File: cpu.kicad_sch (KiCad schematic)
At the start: 1 part, among them U1 Intel_8088

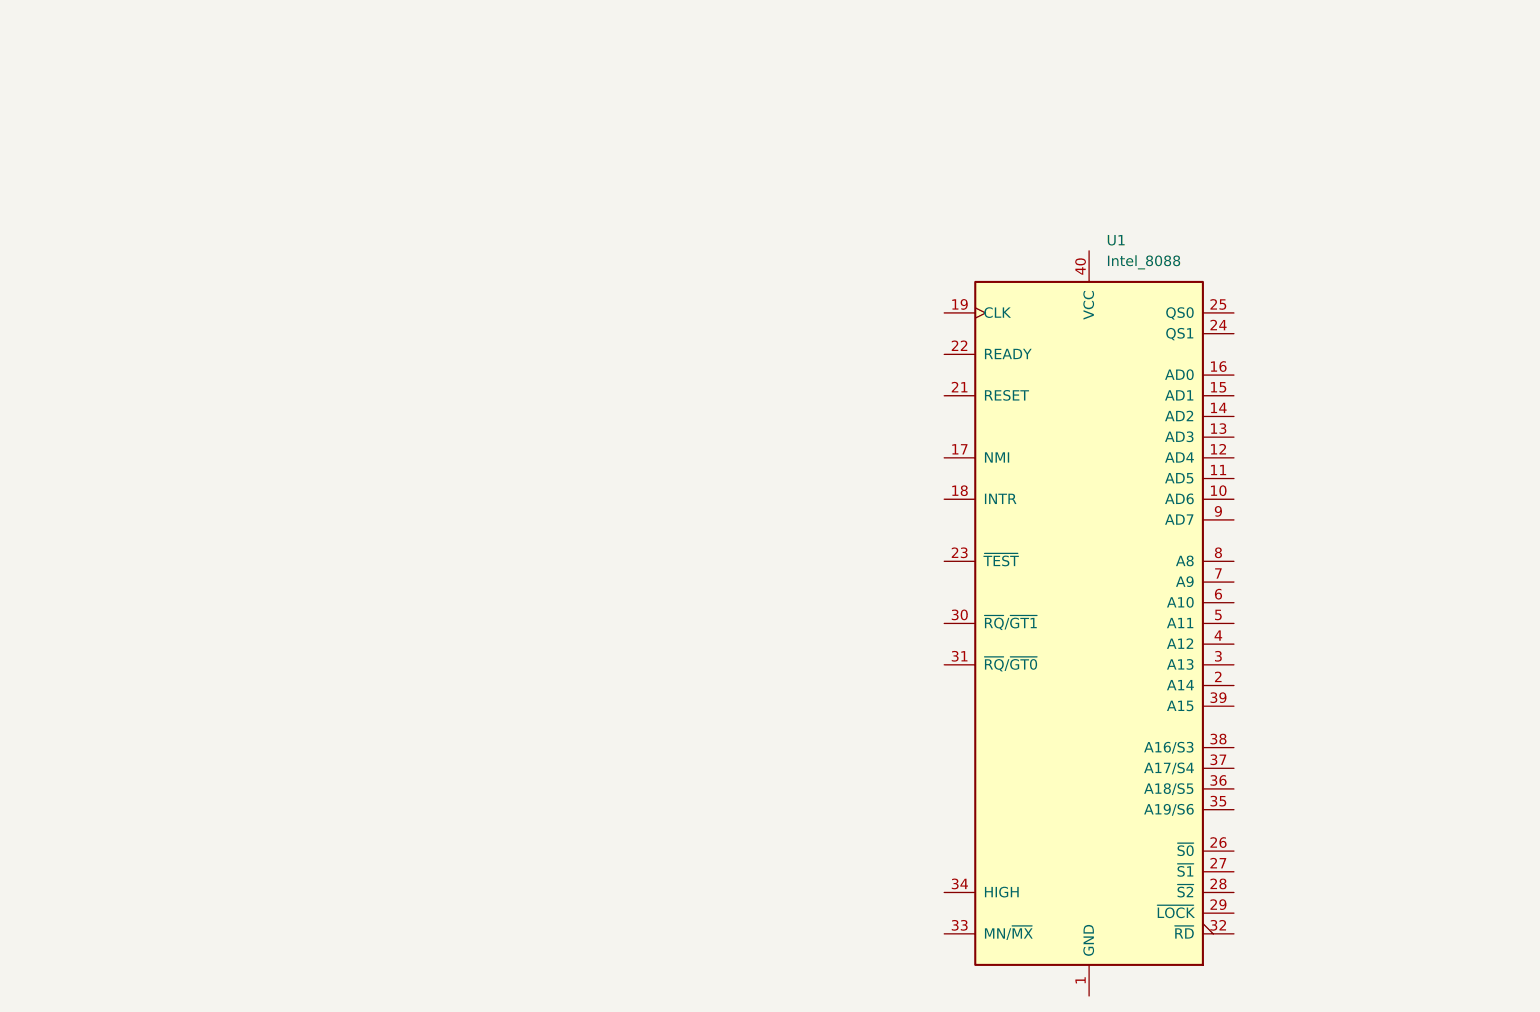
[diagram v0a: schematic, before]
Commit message: cpu and fpu connected together
Signed-off-by: Lucy Mielke <user@domain.tld>
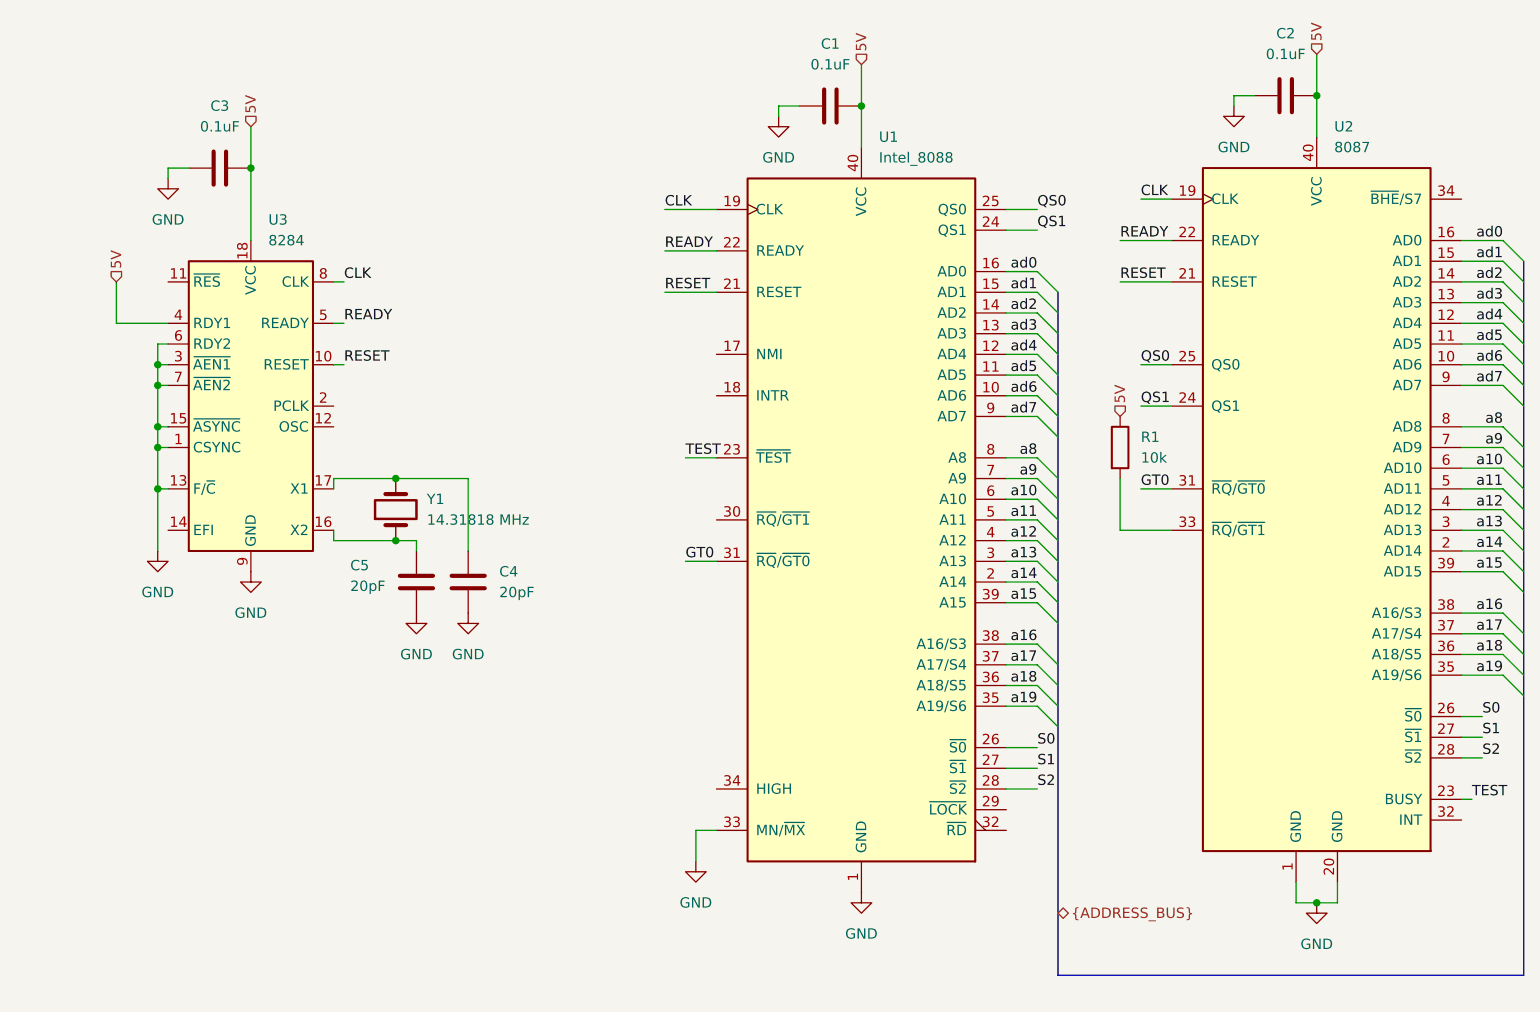
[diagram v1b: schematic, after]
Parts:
- added C1, C2, C3: 0.1uF, Capacitor_THT:C_Disc_D3.0mm_W1.6mm_P2.50mm, symbol Device:C
- added C4, C5: 20pF, Capacitor_THT:C_Disc_D3.0mm_W1.6mm_P2.50mm, symbol Device:C
- added R1: 10k, Resistor_THT:R_Axial_DIN0204_L3.6mm_D1.6mm_P5.08mm_Horizontal, symbol Device:R
- added U2: 8087, Package_DIP:DIP-40_W15.24mm_Socket, symbol MCU_Intel:8087
- added U3: 8284, Package_DIP:DIP-18_W7.62mm_Socket, symbol Timer:8284
- added Y1: 14.31818 MHz, Crystal:Crystal_HC49-U_Vertical, symbol Device:Crystal
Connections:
- net GND: now reaches U1.1 (GND), U1.20 (GND)
- net GND: now also U1.33 (MN/~{MX}), C1.1, C2.1, C3.1, C4.1, C5.2, U2.1 (GND), U2.20 (GND), U3.1 (CSYNC), U3.13 (F/~{C}), U3.15 (~{ASYNC}), U3.3 (~{AEN1}), U3.6 (RDY2), U3.7 (~{AEN2}), U3.9 (GND)
- net ad6: now reaches U1.10 (AD6)
- net ad6: now also U2.10 (AD6)
- net ad5: now reaches U1.11 (AD5)
- net ad5: now also U2.11 (AD5)
- net ad4: now reaches U1.12 (AD4)
- net ad4: now also U2.12 (AD4)
- net ad3: now reaches U1.13 (AD3)
- net ad3: now also U2.13 (AD3)
- net ad2: now reaches U1.14 (AD2)
- net ad2: now also U2.14 (AD2)
- net ad1: now reaches U1.15 (AD1)
- net ad1: now also U2.15 (AD1)
- net ad0: now reaches U1.16 (AD0)
- net ad0: now also U2.16 (AD0)
- net CLK: now reaches U1.19 (CLK)
- net CLK: now also U2.19 (CLK), U3.8 (CLK)
- net a14: now reaches U1.2 (A14)
- net a14: now also U2.2 (AD14)
- net RESET: now reaches U1.21 (RESET)
- net RESET: now also U2.21 (RESET), U3.10 (RESET)
- net READY: now reaches U1.22 (READY)
- net READY: now also U2.22 (READY), U3.5 (READY)
- net TEST: now reaches U1.23 (~{TEST})
- net TEST: now also U2.23 (BUSY)
- net QS1: now reaches U1.24 (QS1)
- net QS1: now also U2.24 (QS1)
- net QS0: now reaches U1.25 (QS0)
- net QS0: now also U2.25 (QS0)
- net S0: now reaches U1.26 (~{S0})
- net S0: now also U2.26 (~{S0})
- net S1: now reaches U1.27 (~{S1})
- net S1: now also U2.27 (~{S1})
- net S2: now reaches U1.28 (~{S2})
- net S2: now also U2.28 (~{S2})
- net a13: now reaches U1.3 (A13)
- net a13: now also U2.3 (AD13)
- net GT0: now reaches U1.31 (~{RQ}/~{GT0})
- net GT0: now also U2.31 (~{RQ}/~{GT0})
- net a19: now reaches U1.35 (A19/S6)
- net a19: now also U2.35 (A19/S6)
- net a18: now reaches U1.36 (A18/S5)
- net a18: now also U2.36 (A18/S5)
- net a17: now reaches U1.37 (A17/S4)
- net a17: now also U2.37 (A17/S4)
- net a16: now reaches U1.38 (A16/S3)
- net a16: now also U2.38 (A16/S3)
- net a15: now reaches U1.39 (A15)
- net a15: now also U2.39 (AD15)
- net a12: now reaches U1.4 (A12)
- net a12: now also U2.4 (AD12)
- net 5V: now reaches U1.40 (VCC)
- net 5V: now also C1.2, C2.2, C3.2, R1.1, U2.40 (VCC), U3.18 (VCC), U3.4 (RDY1)
- net a11: now reaches U1.5 (A11)
- net a11: now also U2.5 (AD11)
- net a10: now reaches U1.6 (A10)
- net a10: now also U2.6 (AD10)
- net a9: now reaches U1.7 (A9)
- net a9: now also U2.7 (AD9)
- net a8: now reaches U1.8 (A8)
- net a8: now also U2.8 (AD8)
- net ad7: now reaches U1.9 (AD7)
- net ad7: now also U2.9 (AD7)
- new net: R1.2, U2.33 (~{RQ}/~{GT1})
- new net: C5.1, U3.16 (X2), Y1.1
- new net: C4.2, U3.17 (X1), Y1.2
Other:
- moved on the sheet: U1

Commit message: power delivery to compute basics
Signed-off-by: Lucy Mielke <user@domain.tld>
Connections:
- net RSTBTN: now reaches U3.11 (~{RES})
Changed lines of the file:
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@@
 	(wire
 		(pts
-			(xy 138.43 110.49) (xy 142.24 110.49)
+			(xy 138.43 110.49) (xy 139.7 110.49)
 		)
 		(stroke
@@
 	(wire
 		(pts
+			(xy 26.67 50.8) (xy 35.56 50.8)
+		)
+		(stroke
+			(width 0)
+			(type default)
+		)
+	)
+	(wire
+		(pts
 			(xy 142.24 59.69) (xy 138.43 59.69)
 		)
@@
 	(wire
 		(pts
-			(xy 29.21 50.8) (xy 29.21 55.88)
+			(xy 29.21 46.99) (xy 29.21 55.88)
 		)
 		(stroke
@@
 	(wire
 		(pts
-			(xy 138.43 113.03) (xy 142.24 113.03)
+			(xy 138.43 113.03) (xy 139.7 113.03)
 		)
 		(stroke
@@
 	(wire
 		(pts
-			(xy 138.43 107.95) (xy 142.24 107.95)
+			(xy 138.43 107.95) (xy 139.7 107.95)
 		)
 		(stroke
@@
 	)
 	(label "S2"
-		(at 142.24 113.03 0)
+		(at 139.7 113.03 0)
 		(effects
 			(font
@@
 	)
 	(label "S1"
-		(at 142.24 110.49 0)
+		(at 139.7 110.49 0)
 		(effects
 			(font
@@
 	)
 	(label "S0"
-		(at 142.24 107.95 0)
+		(at 139.7 107.95 0)
 		(effects
 			(font
@@
 		)
 	)
+	(hierarchical_label "RSTBTN"
+		(shape input)
+		(at 26.67 50.8 180)
+		(effects
+			(font
+				(size 1.27 1.27)
+			)
+			(justify right)
+		)
+	)
 	(hierarchical_label "5V"
 		(shape input)
-		(at 29.21 50.8 90)
-		(effects
-			(font
+		(at 29.21 46.99 90)
+		(effects
+			(font
